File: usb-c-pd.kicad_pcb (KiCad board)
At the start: 2 copper layers, 4.5 x 13.4 mm, 52 parts, among them J1 USB_C_Receptacle_USB2.0_14P, J2 Barrel_Jack_Switch, J3 Conn_ARM_SWD_TagConnect_TC203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, Q1 T2N7002AK, U1 CYPD3177-24LQ, U2 STM32C071F8Px, U3 INA180A2, U4 XL1509-3.3

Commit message: feat: routing
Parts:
- J1: footprint Connector_USB:USB_C_Receptacle_Amphenol_12401948E412A -> usb-c-pd-lib:GCT_USB4105-GF-A
- moved R20 42.4 mm to (44.2, 66.2)
- moved R22 39.5 mm to (42.2, 66.2)
- moved R21 37.4 mm to (46.5, 68.0)
- moved C8 34.1 mm to (71.0, 87.5), turned to 90 degrees
- moved C9 26.7 mm to (68.0, 88.5), turned to 180 degrees
- moved R15 26.5 mm to (35.0, 96.0)
- moved Q1 25.5 mm to (37.5, 76.5)
- moved U3 25.2 mm to (69.7, 92.0), turned to 0 degrees
- moved C13 25.1 mm to (65.5, 81.0), turned to -90 degrees
- moved C14 24.1 mm to (62.0, 77.0), turned to 180 degrees
- moved R19 22.2 mm to (65.0, 89.5)
- moved C7 20.9 mm to (43.0, 102.2), turned to 180 degrees
- moved R5 20.8 mm to (43.5, 82.2)
- moved D1 19.7 mm to (41.0, 76.5), turned to -90 degrees
- moved R2 19.6 mm to (37.5, 73.5)
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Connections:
- net Net-(J1-CC1) renamed CC1
- net Net-(J1-CC2) renamed CC2
- R1 pad 2: +3V3 -> +3V3 MCU
- R3 pad 1: +3V3 -> +3V3 MCU
- R4 pad 1: +3V3 -> +3V3 MCU
- U2 pad 2: PD_GPIO -> HPI_INT
- U2 pad 3: HPI_INT -> PD_GPIO
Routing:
- net +3V3 MCU: track 0.00 -> 87.7 mm, vias 0 -> 6
- net VBUS: track 0.00 -> 44.3 mm, vias 0 -> 3
- net Net-(C6-Pad2): track 0.00 -> 37.5 mm, vias 0 -> 2
- net AMP_OUT: track 0.00 -> 32.8 mm, vias 0 -> 4
- net GND: track 0.00 -> 27.1 mm, vias 0 -> 39
- net +VBUS_PD: track 0.00 -> 25.1 mm, vias 0 -> 2
- net USB_DP: track 0.00 -> 22.2 mm, vias 0 -> 2
- net Net-(Q1-G): track 0.00 -> 21.3 mm, vias 0 -> 2
- net USB_DM: track 0.00 -> 20.2 mm
- net PD_SAFE: track 0.00 -> 19.7 mm, vias 0 -> 4
- net PD_FLIP: track 0.00 -> 16.3 mm, vias 0 -> 2
- net PD_GPIO: track 0.00 -> 15.2 mm
- net HPI_INT: track 0.00 -> 15.1 mm
- net SWCLK: track 0.00 -> 14.5 mm, vias 0 -> 2
- net SWDIO: track 0.00 -> 12.6 mm
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- added copper zone on F.Cu, net +VBUS_PD
- added copper zone on B.Cu, net GND
- added copper zone on F.Cu, net VBUS
- added copper zone on F.Cu, net VCONN
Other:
- board size 4.5 x 13.4 mm -> 58.8 x 42.2 mm

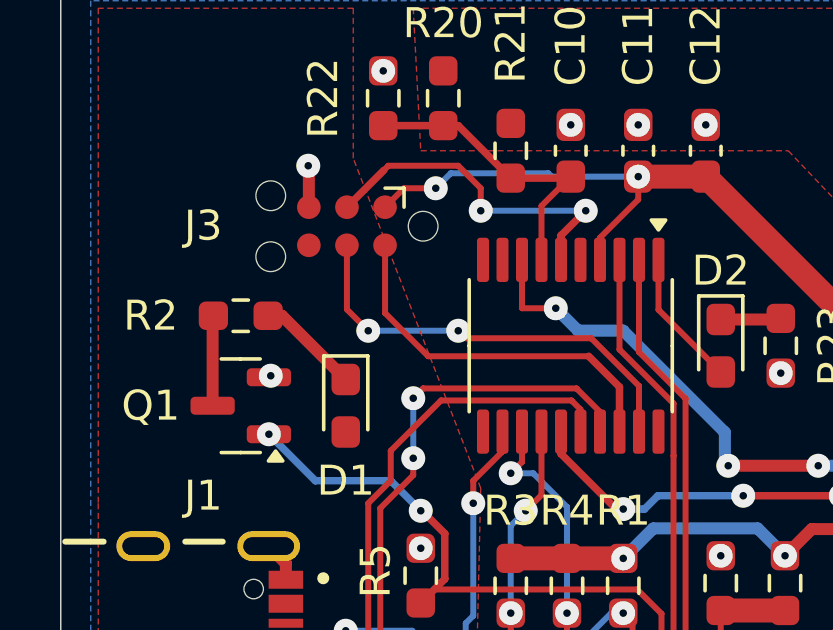
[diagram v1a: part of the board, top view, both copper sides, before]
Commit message: feat: add 3d models and diode R values
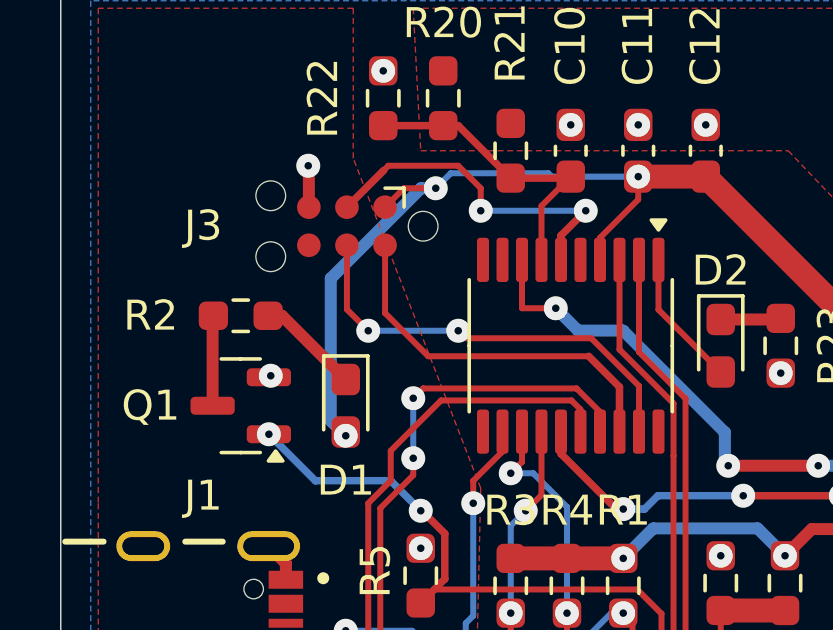
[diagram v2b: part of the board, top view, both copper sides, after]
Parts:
- R2, R23: value TODO -> 165
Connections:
- D1 pad 2: VBUS -> +3V3 MCU
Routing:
- net +3V3 MCU: track 87.7 -> 98.0 mm, vias 6 -> 7
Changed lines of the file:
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@@
 			)
 		)
-		(property "Value" "TODO"
+		(property "Value" "165"
 			(at 0 1.43 0)
 			(layer "F.Fab")
@@
 		)
 		(embedded_fonts no)
+		(model "${KIPRJMOD}/3d_models/DMP3098LSD-13.stp"
+			(offset
+				(xyz 0 0 0)
+			)
+			(scale
+				(xyz 1 1 1)
+			)
+			(rotate
+				(xyz 0 0 0)
+			)
+		)
 	)
 	(footprint "Capacitor_SMD:C_0603_1608Metric_Pad1.08x0.95mm_HandSolder"
@@
 			(layers "F.Cu" "F.Mask" "F.Paste")
 			(roundrect_rratio 0.25)
-			(net 5 "VBUS")
+			(net 8 "+3V3 MCU")
 			(pinfunction "A")
 			(pintype "passive")
@@
 			)
 		)
-		(property "Value" "TODO"
+		(property "Value" "165"
 			(at 0 1.43 90)
 			(layer "F.Fab")
@@
 			)
 		)
+		(model "${KIPRJMOD}/3d_models/CYPD3177-24LQXQT.stp"
+			(offset
+				(xyz 0 0 0)
+			)
+			(scale
+				(xyz 1 1 1)
+			)
+			(rotate
+				(xyz 0 0 0)
+			)
+		)
 	)
 	(footprint "Package_SO:TSSOP-20_4.4x6.5mm_P0.65mm"
@@
 	)
 	(segment
+		(start 41 77.375)
+		(end 41 77.5)
+		(width 0.2)
+		(layer "F.Cu")
+		(net 8)
+	)
+	(segment
 		(start 67.0615 79.199)
 		(end 68.135 78.1255)
@@
 	)
 	(via
+		(at 41 77.5)
+		(size 0.8)
+		(drill 0.25)
+		(layers "F.Cu" "B.Cu")
+		(net 8)
+	)
+	(via
 		(at 44 69.25)
 		(size 0.8)
@@
 	)
 	(segment
+		(start 41 77.5)
+		(end 40.5 77)
+		(width 0.4)
+		(layer "B.Cu")
+		(net 8)
+	)
+	(segment
+		(start 40.5 77)
+		(end 40.5 72.25773)
+		(width 0.4)
+		(layer "B.Cu")
+		(net 8)
+	)
+	(segment
 		(start 54.732065 80.589208)
 		(end 51.248292 80.589208)
@@
 	)
 	(segment
+		(start 40.5 72.25773)
+		(end 43.50773 69.25)
+		(width 0.4)
+		(layer "B.Cu")
+		(net 8)
+	)
+	(segment
 		(start 47.8625 68.8625)
 		(end 50.75 68.8625)
@@
 		(width 0.4)
 		(layer "B.Cu")
+		(net 8)
+	)
+	(segment
+		(start 43.50773 69.25)
+		(end 44 69.25)
+		(width 0.4)
+		(layer "B.Cu")

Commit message: feat: finalize design
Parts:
- added H1: MountingHole_Pad, MountingHole:MountingHole_3.2mm_M3_DIN965_Pad, F.Cu at (61.5, 67.2)
- added H2: MountingHole_Pad, MountingHole:MountingHole_3.2mm_M3_DIN965_Pad, F.Cu at (84.2, 101.5)
- moved L1 10.5 mm to (61.5, 73.5), turned to 180 degrees
- moved D3 1.95 mm to (61.5, 75.2), turned to 180 degrees
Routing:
- net Net-(D3-K): track 12.3 -> 7.53 mm
- net +3V3 MCU: track 98.0 -> 95.3 mm
- net USB_DP: track 22.2 -> 22.9 mm
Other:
- board size 58.8 x 42.2 mm -> 58.8 x 43 mm
